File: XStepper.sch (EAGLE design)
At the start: 97 parts, among them IC1 L7805, IC2 L7812, Q2 16 MHZ, U1 FT232RL-BASICSSOP

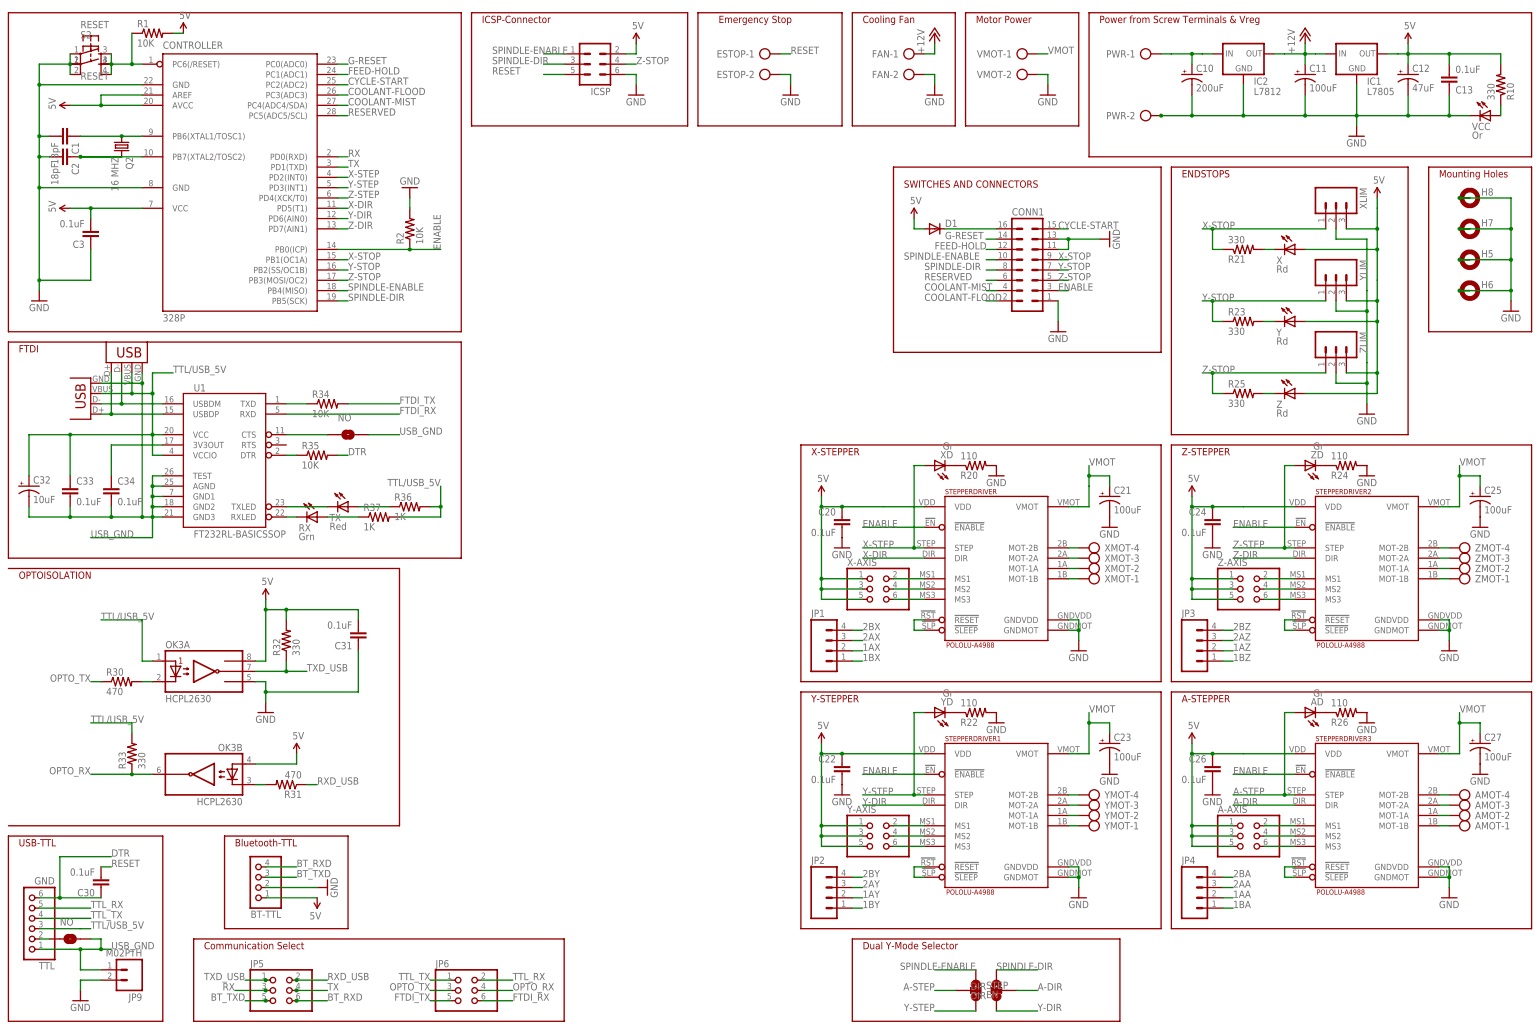
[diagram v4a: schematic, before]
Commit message: - version 0.97 to fab
*On-board USB in now in the bottom of the board
*USB isolation header moved.
*Bluetooth header moved
*Bluetooth dip/jumpers removed - bluetooth is always-on
*FTDI header moved
*FTDI now can be tied to 5V and GND for isolation or to forego isolation
and directly power the board logic from USB
*Pololu jumpers now separated (I forgot that this was a requirement and
not an option)
*Removed endstop status LED's
*Removed 16-pin header
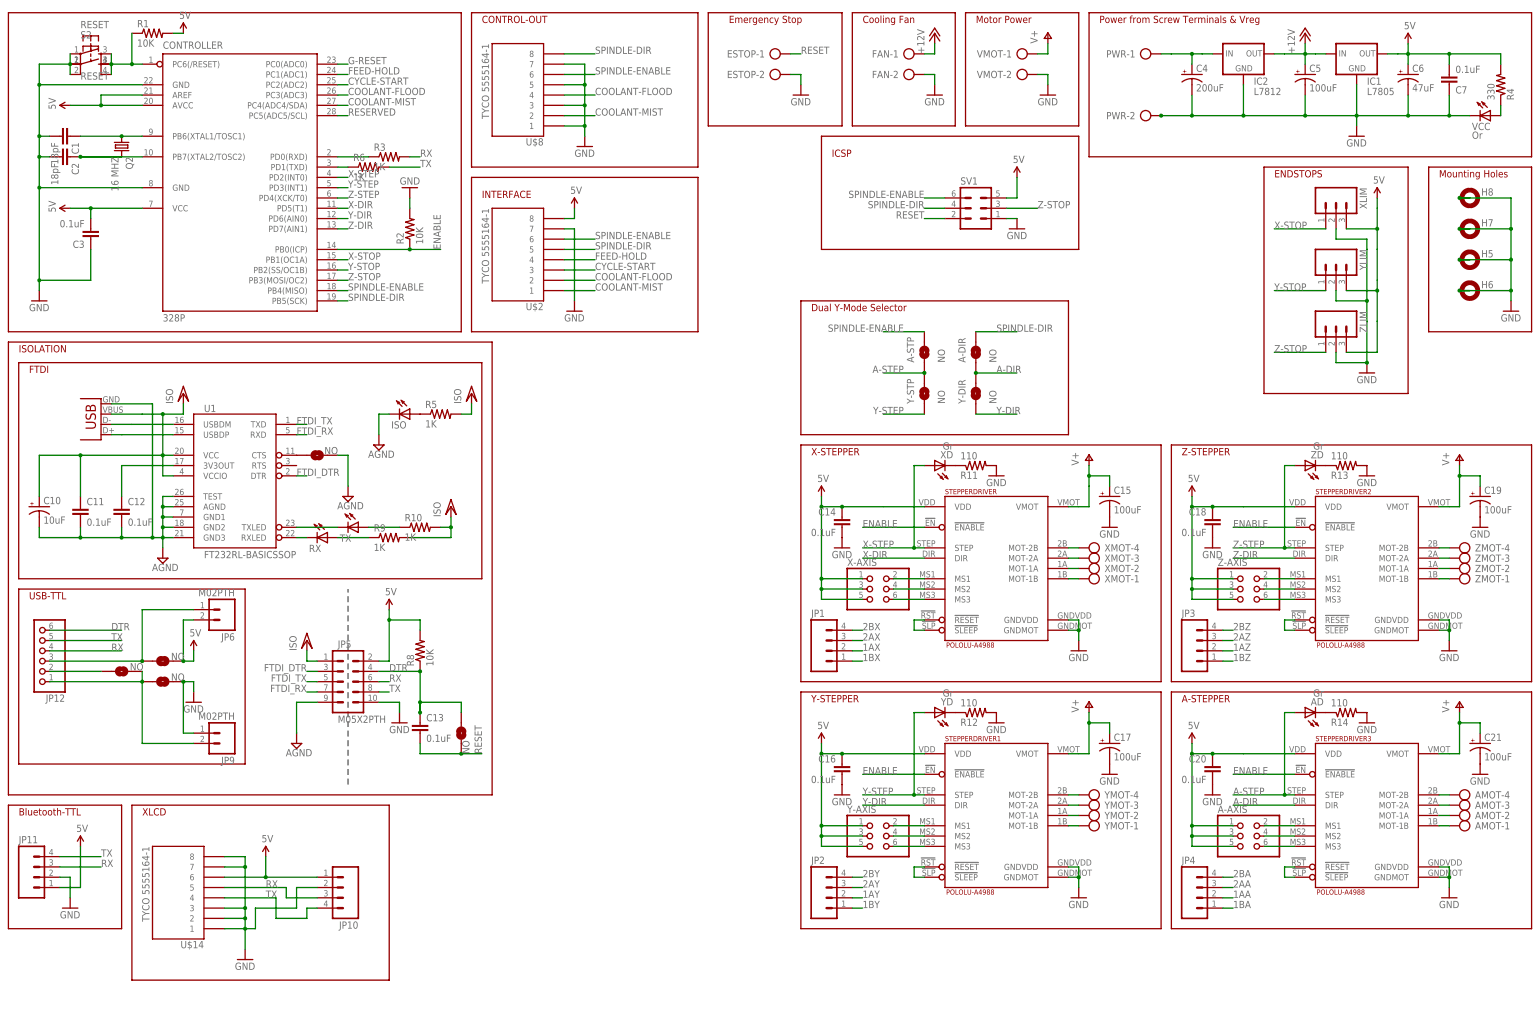
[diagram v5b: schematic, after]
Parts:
- removed BT-TTL: (no value), pinhead:PINHD-1X4
- removed C26, C30, C31: 0.1uF, resistor:C-EU025-025X050
- removed C27: 100uF, resistor:CPOL-USE3.5-8
- removed C32: 10uF, SparkFun-Capacitors:CAP_POL1206
- removed C33, C34: 0.1uF, SparkFun-Capacitors:CAP1206
- removed CONN1: (no value), con-ml:ML16
- removed D1: (no value), SparkFun-DiscreteSemi:DIODEPTH
- removed DIR: DIR, SparkFun-Passives:SOLDERJUMPER_2WAYW
- removed ICSP: (no value), con-ml:ML6
- removed JP8: USB-B, SparkFun-Connectors:USBPTH
- removed OK3: HCPL2630, optocoupler:HCPL2630
- removed R21, R23, R25, R32, R33: 330, SparkFun-Resistors:RESISTORAXIAL-0.3
- removed R30, R31: 470, SparkFun-Resistors:RESISTORAXIAL-0.3
- removed R34, R35: 10K, SparkFun-Resistors:RESISTOR1206
- removed R36, R37: 1K, SparkFun-Resistors:RESISTOR1206
- removed SJ1, SJ4: NO, SparkFun-Passives:SOLDERJUMPERNO
- removed STEP: EN, SparkFun-Passives:SOLDERJUMPER_2WAYW
- removed TTL: GND, pinhead:PINHD-1X6
- removed X, Y, Z: Rd, SparkFun-LED:LED3MM
- added 5V, A-DIR, A-STP, CTS, CTS-FTDI, DTR, GND, Y-DIR, Y-STP: NO, SparkFun-Passives:SOLDERJUMPERNO
- added C14, C7: 0.1uF, resistor:C-EU025-025X050
- added C15: 100uF, resistor:CPOL-USE3.5-8
- added C4: 200uF, resistor:CPOL-USE3.5-8
- added C5: 100uF, resistor:CPOL-USE2.5-6
- added C6: 47uF, resistor:CPOL-USE2.5-6
- added ISO: (no value), SparkFun-LED:LED3MM
- added JP10, JP11: (no value), SparkFun-Connectors:M04PTH
- added JP12: (no value), pinhead:PINHD-1X6
- added R3, R6: 1K, SparkFun-Resistors:RESISTORAXIAL-0.3
- added R4: 330, SparkFun-Resistors:RESISTORAXIAL-0.3
- added R5, R9: 1K, SparkFun-Resistors:RESISTOR1206
- added R8: 10K, SparkFun-Resistors:RESISTORAXIAL-0.3
- added SV1: (no value), con-ml:ML6
- added U$14, U$2, U$8: TYCO 5555164-1, SparkFun-Connectors:RJ45-8PTH
- C10: value 200uF -> 10uF; device resistor:CPOL-USE3.5-8 -> SparkFun-Capacitors:CAP_POL1206
- C11: value 100uF -> 0.1uF; device resistor:CPOL-USE2.5-6 -> SparkFun-Capacitors:CAP1206
- C12: value 47uF -> 0.1uF; device resistor:CPOL-USE2.5-6 -> SparkFun-Capacitors:CAP1206
- JP5: value (none) -> M05X2PTH; device pinhead:PINHD-2X3 -> SparkFun-Connectors:M05X2PTH
- JP6: value (none) -> M02PTH; device pinhead:PINHD-2X3 -> SparkFun-Connectors:M02PTH
- R10: value 330 -> 1K; device SparkFun-Resistors:RESISTORAXIAL-0.3 -> SparkFun-Resistors:RESISTOR1206
- RX: value Grn -> (none); device SparkFun-LED:LED1206 -> SparkFun-LED:LED3MM
- TX: value Red -> (none); device SparkFun-LED:LED1206 -> SparkFun-LED:LED3MM
- renumbered C22 to C16, C23 to C17, C24 to C18, C25 to C19, R20 to R11, R22 to R12, R24 to R13, R26 to R14
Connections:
- removed net BT_RXD: BT-TTL.4, JP5.6
- removed net BT_TXD: BT-TTL.3, JP5.5
- removed net N$35: R21.2, X.C
- removed net N$36: R23.2, Y.C
- removed net N$37: R25.2, Z.C
- removed net N$45: CONN1.16, D1.C
- removed net N$46: OK3B.C2, R31.2
- removed net N$47: OK3A.C1, R30.2
- removed net OPTO_RX: JP6.4, OK3B.VO2, R33.1
- removed net OPTO_TX: JP6.3, R30.1
- removed net RXD_USB: JP5.2, R31.1
- removed net TTL/USB_5V: C32.+, C33.1, JP7.VBUS, JP8.VBUS, OK3A.A1, R33.2, R36.2, R37.2, TTL.3, U1.VCC, U1.VCCIO
- removed net TTL_RX: JP6.2, TTL.5
- removed net TTL_TX: JP6.1, TTL.4
- removed net TXD_USB: JP5.1, OK3A.VO1, R32.1
- removed net USB_GND: C32.-, C33.2, C34.2, JP7.GND, JP8.GND, JP9.1, SJ1.2, SJ4.2, TTL.1, U1.AGND, U1.GND1, U1.GND2, U1.GND3, U1.TEST
- removed net VMOT: C17.+, C19.+, C21.+, C27.+, STEPPERDRIVER.VMOT, STEPPERDRIVER1.VMOT, STEPPERDRIVER2.VMOT, STEPPERDRIVER3.VMOT, VMOT-1.KL
- new net AGND: C10.-, C11.2, C12.2, CTS-FTDI.2, ISO.C, JP5.9, JP7.GND, U1.AGND, U1.GND1, U1.GND2, U1.GND3, U1.TEST
- new net FTDI_DTR: JP5.3, U1.DTR
- new net N$40: 328P.PD1(TXD), R6.1
- new net N$41: 5V.1, JP12.3, JP6.1
- new net N$44: CTS.2, GND.1, JP12.1, JP9.2
- new net V+: C15.+, C17.+, C19.+, C21.+, STEPPERDRIVER.VMOT, STEPPERDRIVER1.VMOT, STEPPERDRIVER2.VMOT, STEPPERDRIVER3.VMOT, VMOT-1.KL
- new net VCC/2: C10.+, C11.1, JP5.1, JP7.VBUS, R10.2, R5.2, R9.2, U1.VCC, U1.VCCIO
- net +12V: now also C5.+; no longer C11.+
- net 5V: now also 5V.2, C14.1, C6.+, C7.2, JP10.1, JP11.1, JP5.2, JP6.2, R4.2, R8.2, SV1.5, U$14.6, U$2.8; no longer BT-TTL.1, C12.+, C13.2, C26.1, C31.2, D1.A, ICSP.2, OK3A.VCC, OK3B.A2, R10.2, R32.2, X.A, Y.A, Z.A
- net A-DIR: now also A-DIR.1, Y-DIR.2; no longer DIR.2
- net A-STEP: now also A-STP.1, Y-STP.2; no longer STEP.2
- net COOLANT-FLOOD: now also U$2.2, U$8.4; no longer CONN1.2
- net COOLANT-MIST: now also U$2.1, U$8.2; no longer CONN1.4
- net CYCLE-START: now also U$2.3; no longer CONN1.15
- net DTR: now also C13.1, DTR.1, JP12.6, JP5.4, R8.1; no longer C30.1, R35.2, TTL.6
- net ENABLE: no longer CONN1.3
- net FEED-HOLD: now also U$2.4; no longer CONN1.12
- net FTDI_RX: now also JP5.7; no longer JP6.6
- net FTDI_TX: now also JP5.5, U1.TXD; no longer JP6.5, R34.2
- net G-RESET: no longer CONN1.14
- net GND: now also C14.2, C15.-, C4.-, C5.-, C6.-, C7.1, GND.2, JP10.2, JP11.2, JP5.10, JP9.1, SV1.1, U$14.1, U$14.2, U$14.3, U$14.7, U$14.8, U$2.7, U$8.1, U$8.3, U$8.5, U$8.7; no longer BT-TTL.2, C10.-, C11.-, C12.-, C13.1, C26.2, C27.-, C31.1, CONN1.1, CONN1.11, CONN1.13, ICSP.6, JP9.2, OK3A.GND
- net N$1: now also C12.1; no longer C34.1
- net N$10: now also CTS.1, JP12.2; no longer SJ1.1, TTL.2
- net N$17: now also R9.1; no longer R37.1
- net N$18: now also R10.1; no longer R36.1
- net N$19: now also CTS-FTDI.1; no longer SJ4.1
- net N$2: no longer JP8.D+
- net N$3: no longer JP8.D-
- net N$4: now also ISO.A, R5.1; no longer R35.1, U1.DTR
- net N$43: now also R4.1; no longer R10.1
- net N$9: now also 328P.PD0(RXD), R3.1; no longer R34.1, U1.TXD
- net RESERVED: no longer CONN1.6
- net RESET: now also C13.2, DTR.2, SV1.2; no longer C30.2, ICSP.5
- net RX: now also JP10.3, JP11.3, JP12.4, JP5.6, R3.2, U$14.5; no longer 328P.PD0(RXD), JP5.3
- net SPINDLE-DIR: now also A-DIR.2, SV1.4, U$2.5, U$8.8; no longer CONN1.8, DIR.3, ICSP.3
- net SPINDLE-ENABLE: now also A-STP.2, SV1.6, U$2.6, U$8.6; no longer CONN1.10, ICSP.1, STEP.1
- net TX: now also JP10.4, JP11.4, JP12.5, JP5.8, R6.2, U$14.4; no longer 328P.PD1(TXD), JP5.4
- net VIN: now also C4.+; no longer C10.+
- net X-STOP: no longer CONN1.9, R21.1
- net Y-DIR: now also Y-DIR.1; no longer DIR.1
- net Y-STEP: now also Y-STP.1; no longer STEP.3
- net Y-STOP: no longer CONN1.7, R23.1
- net Z-STOP: now also SV1.3; no longer CONN1.5, ICSP.4, R25.1
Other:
- note added: "CONTROL-OUT"
- note added: "ICSP"
- note added: "INTERFACE"
- note added: "ISOLATION"
- note added: "XLCD"
- note removed: "Communication Select"
- note removed: "ICSP-Connector"
- note removed: "OPTOISOLATION"
- note removed: "SWITCHES AND CONNECTORS"
- moved on the sheet: C10, C13, C20, C21, ESTOP-1, ESTOP-2, JP9, R10, RX, TX, U1, YLIM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
